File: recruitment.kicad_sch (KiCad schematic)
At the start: 1 part

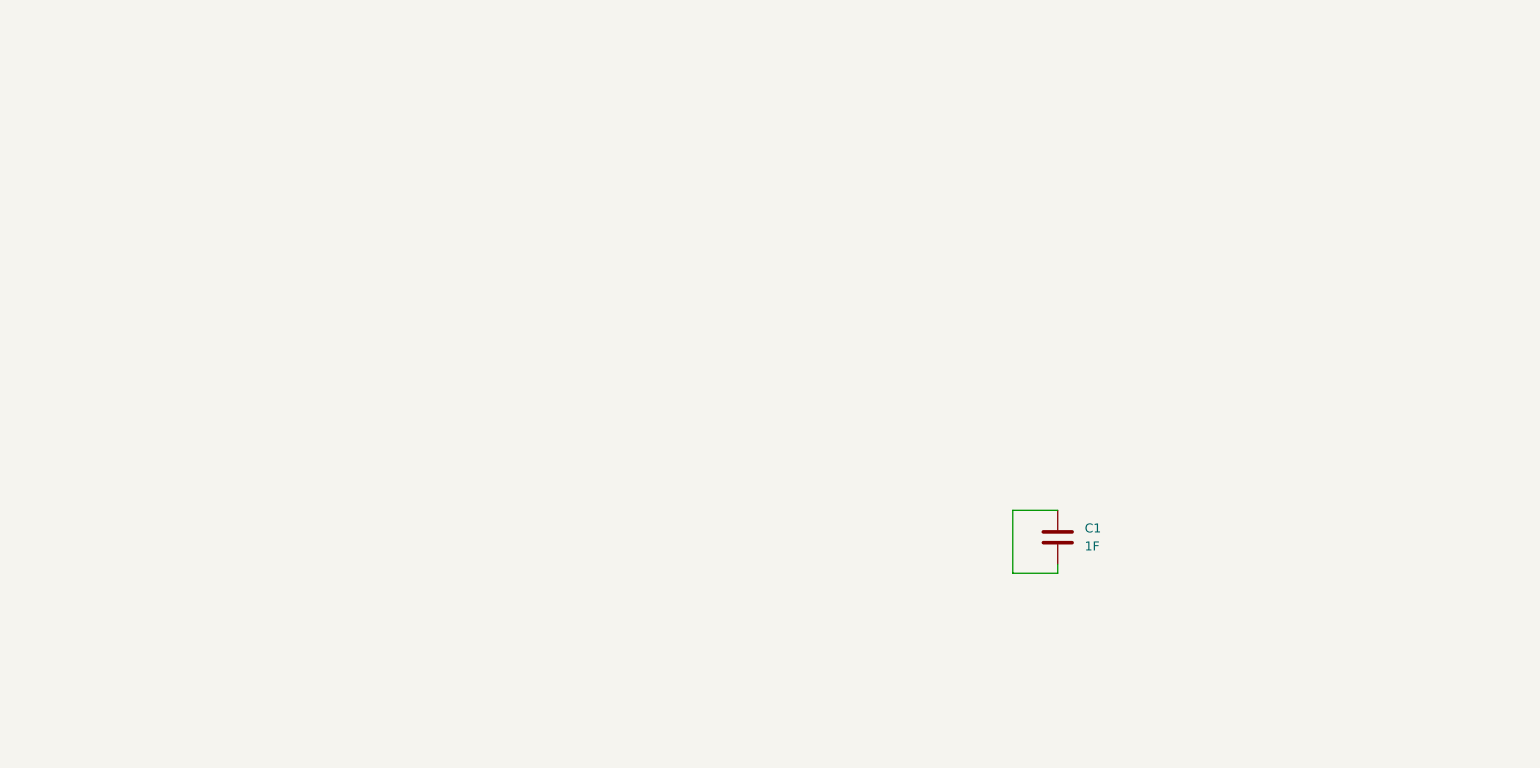
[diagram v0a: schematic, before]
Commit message: feat:added hierarchical sheets and hierarchical labels for input and output
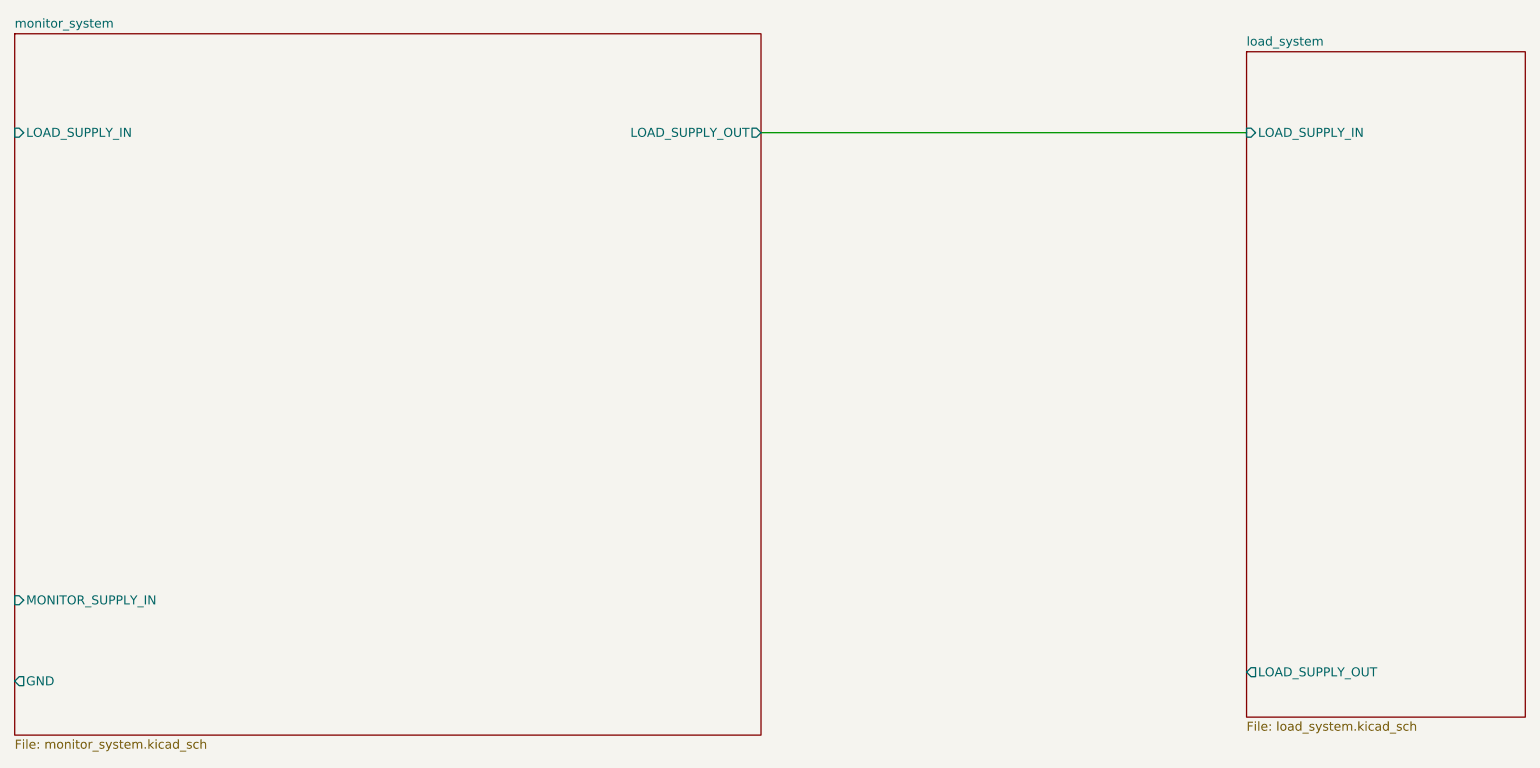
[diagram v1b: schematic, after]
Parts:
- removed C1: 1F, Capacitor_SMD:C_0805_2012Metric, symbol Device:C
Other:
- added sheet load_system (load_system.kicad_sch)
- added sheet monitor_system (monitor_system.kicad_sch)
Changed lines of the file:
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@@
-(kicad_sch (version 20211123) (generator eeschema)
-  (paper "A4")
-  (title_block
-    (title "Template")
-    (date "2022-04-19")
-    (rev "V0")
-    (company "E-Agle TRT")
-  )
-  (wire (pts (xy 199.39 121.92) (xy 193.04 121.92))
-    (stroke (width 0) (type default) (color 0 0 0 0))
-  )
-  (wire (pts (xy 193.04 121.92) (xy 193.04 130.81))
-    (stroke (width 0) (type default) (color 0 0 0 0))
-  )
-  (wire (pts (xy 199.39 130.81) (xy 199.39 129.54))
-    (stroke (width 0) (type default) (color 0 0 0 0))
-  )
-  (wire (pts (xy 193.04 130.81) (xy 199.39 130.81))
-    (stroke (width 0) (type default) (color 0 0 0 0))
-  )
-  (symbol (lib_id "Device:C") (at 199.39 125.73 0) (unit 1)
-    (in_bom yes) (on_board yes) (fields_autoplaced)
-    (property "Reference" "C1" (id 0) (at 203.2 124.4599 0)
-      (effects (font (size 1.27 1.27)) (justify left))
-    )
-    (property "Value" "1F" (id 1) (at 203.2 126.9999 0)
-      (effects (font (size 1.27 1.27)) (justify left))
-    )
-    (property "Footprint" "Capacitor_SMD:C_0805_2012Metric" (id 2) (at 200.3552 129.54 0)
-      (effects (font (size 1.27 1.27)) hide)
-    )
-    (property "Datasheet" "~" (id 3) (at 199.39 125.73 0)
-      (effects (font (size 1.27 1.27)) hide)
-    )
-    (pin "1")
-    (pin "2")
-  )
-  (sheet_instances
-    (path "/" (page "1"))
-  )
-  (symbol_instances
-    (path "/34d03349-6d78-4165-a683-2d8b76f2bae8"
-      (reference "C1") (unit 1) (value "1F") (footprint "Capacitor_SMD:C_0805_2012Metric")
-    )
-  )
+(kicad_sch
+	(version 20250114)
+	(generator "eeschema")
+	(generator_version "9.0")
+	(paper "A4")
+	(title_block
+		(title "Template")
+		(date "2022-04-19")
+		(rev "V0")
+		(company "E-Agle TRT")
+	)
+	(wire
+		(pts
+			(xy 157.48 68.58) (xy 226.06 68.58)
+		)
+		(stroke
+			(width 0)
+			(type default)
+		)
+	)
+	(sheet
+		(at 52.07 54.61)
+		(size 105.41 99.06)
+		(exclude_from_sim no)
+		(in_bom yes)
+		(on_board yes)
+		(dnp no)
+		(fields_autoplaced yes)
+		(stroke
+			(width 0.1524)
+			(type solid)
+		)
+		(fill
+			(color 0 0 0 0.0000)
+		)
+		(property "Sheetname" "monitor_system"
+			(at 52.07 53.8984 0)
+			(effects
+				(font
+					(size 1.27 1.27)
+				)
+				(justify left bottom)
+			)
+		)
+		(property "Sheetfile" "monitor_system.kicad_sch"
+			(at 52.07 154.2546 0)
+			(effects
+				(font
+					(size 1.27 1.27)
+				)
+				(justify left top)
+			)
+		)
+		(pin "LOAD_SUPPLY_IN" input
+			(at 52.07 68.58 180)
+			(effects
+				(font
+					(size 1.27 1.27)
+				)
+				(justify left)
+			)
+		)
+		(pin "LOAD_SUPPLY_OUT" output
+			(at 157.48 68.58 0)
+			(effects
+				(font
+					(size 1.27 1.27)
+				)
+				(justify right)
+			)
+		)
+		(pin "GND" output
+			(at 52.07 146.05 180)
+			(effects
+				(font
+					(size 1.27 1.27)
+				)
+				(justify left)
+			)
+		)
+		(pin "MONITOR_SUPPLY_IN" input
+			(at 52.07 134.62 180)
+			(effects
+				(font
+					(size 1.27 1.27)
+				)
+				(justify left)
+			)
+		)
+		(instances
+			(project "recruitment"
+				(path "/bdc7face-9f7c-4701-80bb-4cc144448db1"
+					(page "2")
+				)
+			)
+		)
+	)
+	(sheet
+		(at 226.06 57.15)
+		(size 39.37 93.98)
+		(exclude_from_sim no)
+		(in_bom yes)
+		(on_board yes)
+		(dnp no)
+		(fields_autoplaced yes)
+		(stroke
+			(width 0.1524)
+			(type solid)
+		)
+		(fill
+			(color 0 0 0 0.0000)
+		)
+		(property "Sheetname" "load_system"
+			(at 226.06 56.4384 0)
+			(effects
+				(font
+					(size 1.27 1.27)
+				)
+				(justify left bottom)
+			)
+		)
+		(property "Sheetfile" "load_system.kicad_sch"
+			(at 226.06 151.7146 0)
+			(effects
+				(font
+					(size 1.27 1.27)
+				)
+				(justify left top)
+			)
+		)
+		(pin "LOAD_SUPPLY_IN" input
+			(at 226.06 68.58 180)
+			(effects
+				(font
+					(size 1.27 1.27)
+				)
+				(justify left)
+			)
+		)
+		(pin "LOAD_SUPPLY_OUT" output
+			(at 226.06 144.78 180)
+			(effects
+				(font
+					(size 1.27 1.27)
+				)
+				(justify left)
+			)
+		)
+		(instances
+			(project "recruitment"
+				(path "/bdc7face-9f7c-4701-80bb-4cc144448db1"
+					(page "3")
+				)
+			)
+		)
+	)
+	(sheet_instances
+		(path "/"
+			(page "1")
+		)
+	)
+	(embedded_fonts no)
 )
